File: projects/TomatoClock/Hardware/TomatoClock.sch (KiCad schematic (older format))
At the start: 4 parts, among them U1 ATmega328P-PU, Y1 16MHz

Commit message: TomatoClock: Update hardware schematics
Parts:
- added J1: ICSP, symbol Connector_Generic:Conn_02x03_Odd_Even
- added J2: Screen, Connector_PinHeader_2.00mm:PinHeader_1x04_P2.00mm_Vertical, symbol Connector:Conn_01x04_Male
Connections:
- net +3V3: now also J2.1 (Pin_1)
- net GND: now also J2.2 (Pin_2)
- net SDA: now reaches U1.27 (PC4)
- net SDA: now also J2.3 (Pin_3)
- net SCL: now reaches U1.28 (PC5)
- net SCL: now also J2.4 (Pin_4)
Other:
- note added: "Clock"
- note added: "Peripherals"
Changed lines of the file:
@@
 Wire Notes Line
 	800  750  800  4600
-Wire Notes Line
-	800  4600 4250 4600
-Wire Notes Line
-	4250 4600 4250 750
-Wire Notes Line
-	800  750  4250 750
 Text Notes 3650 4450 0    118  ~ 24
 MCU
+$Comp
+L Connector:Conn_01x04_Male J2
+U 1 1 61928260
+P 5700 1400
+F 0 "J2" H 5672 1374 50  0000 R CNN
+F 1 "Screen" H 5672 1283 50  0000 R CNN
+F 2 "Connector_PinHeader_2.00mm:PinHeader_1x04_P2.00mm_Vertical" H 5700 1400 50  0001 C CNN
+F 3 "~" H 5700 1400 50  0001 C CNN
+	1    5700 1400
+	-1   0    0    -1
+$EndComp
+$Comp
+L power:+3V3 #PWR?
+U 1 1 6192D813
+P 5350 1200
+F 0 "#PWR?" H 5350 1050 50  0001 C CNN
+F 1 "+3V3" H 5365 1373 50  0000 C CNN
+F 2 "" H 5350 1200 50  0001 C CNN
+F 3 "" H 5350 1200 50  0001 C CNN
+	1    5350 1200
+	1    0    0    -1
+$EndComp
+$Comp
+L power:GND #PWR?
+U 1 1 6192DD9D
+P 4900 1500
+F 0 "#PWR?" H 4900 1250 50  0001 C CNN
+F 1 "GND" H 4905 1327 50  0000 C CNN
+F 2 "" H 4900 1500 50  0001 C CNN
+F 3 "" H 4900 1500 50  0001 C CNN
+	1    4900 1500
+	1    0    0    -1
+$EndComp
+Wire Wire Line
+	5350 1200 5350 1300
+Wire Wire Line
+	5350 1300 5500 1300
+Wire Wire Line
+	5500 1400 4900 1400
+Wire Wire Line
+	4900 1400 4900 1500
+Text GLabel 5500 1500 0    39   Input ~ 0
+SDA
+Text GLabel 5500 1600 0    39   Input ~ 0
+SCL
+Wire Notes Line
+	2650 1550 2650 2750
+Wire Notes Line
+	2650 2750 4000 2750
+Wire Notes Line
+	4000 2750 4000 1550
+Wire Notes Line
+	4000 1550 2650 1550
+Text Notes 2700 2700 0    118  ~ 24
+Clock
+Text GLabel 2400 2750 2    39   Input ~ 0
+SDA
+Text GLabel 2400 2850 2    39   Input ~ 0
+SCL
+Wire Notes Line
+	800  4600 4550 4600
+Wire Notes Line
+	4550 750  4550 4600
+Wire Notes Line
+	800  750  4550 750
+$Comp
+L Connector_Generic:Conn_02x03_Odd_Even J1
+U 1 1 6195336E
+P 3650 3800
+F 0 "J1" H 3700 4117 50  0000 C CNN
+F 1 "ICSP" H 3700 4026 50  0000 C CNN
+F 2 "" H 3650 3800 50  0001 C CNN
+F 3 "~" H 3650 3800 50  0001 C CNN
+	1    3650 3800
+	1    0    0    -1
+$EndComp
+Wire Notes Line
+	4650 750  4650 3500
+Wire Notes Line
+	4650 3500 8000 3500
+Wire Notes Line
+	8000 3500 8000 750
+Wire Notes Line
+	8000 750  4650 750
+Text Notes 6900 3400 0    118  ~ 24
+Peripherals
 $EndSCHEMATC

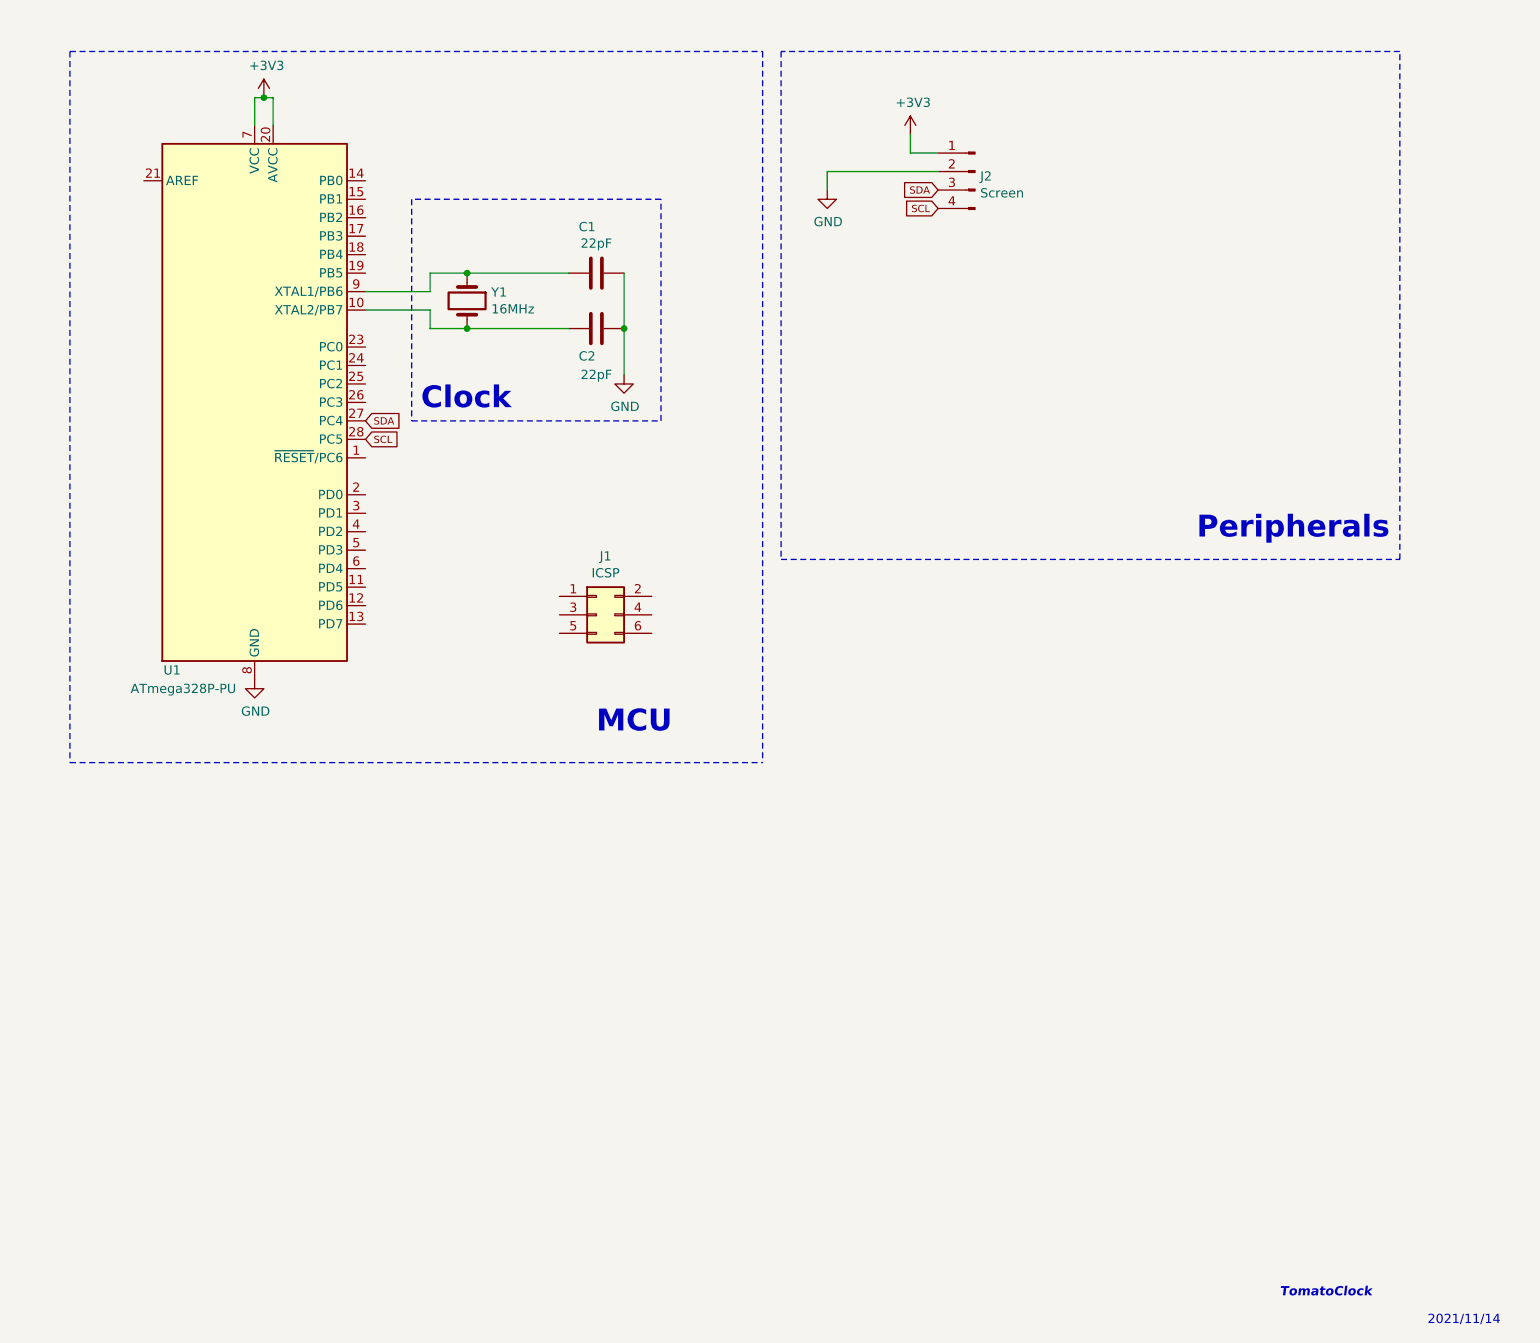
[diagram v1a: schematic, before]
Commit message: TomatoClock: Update hardware
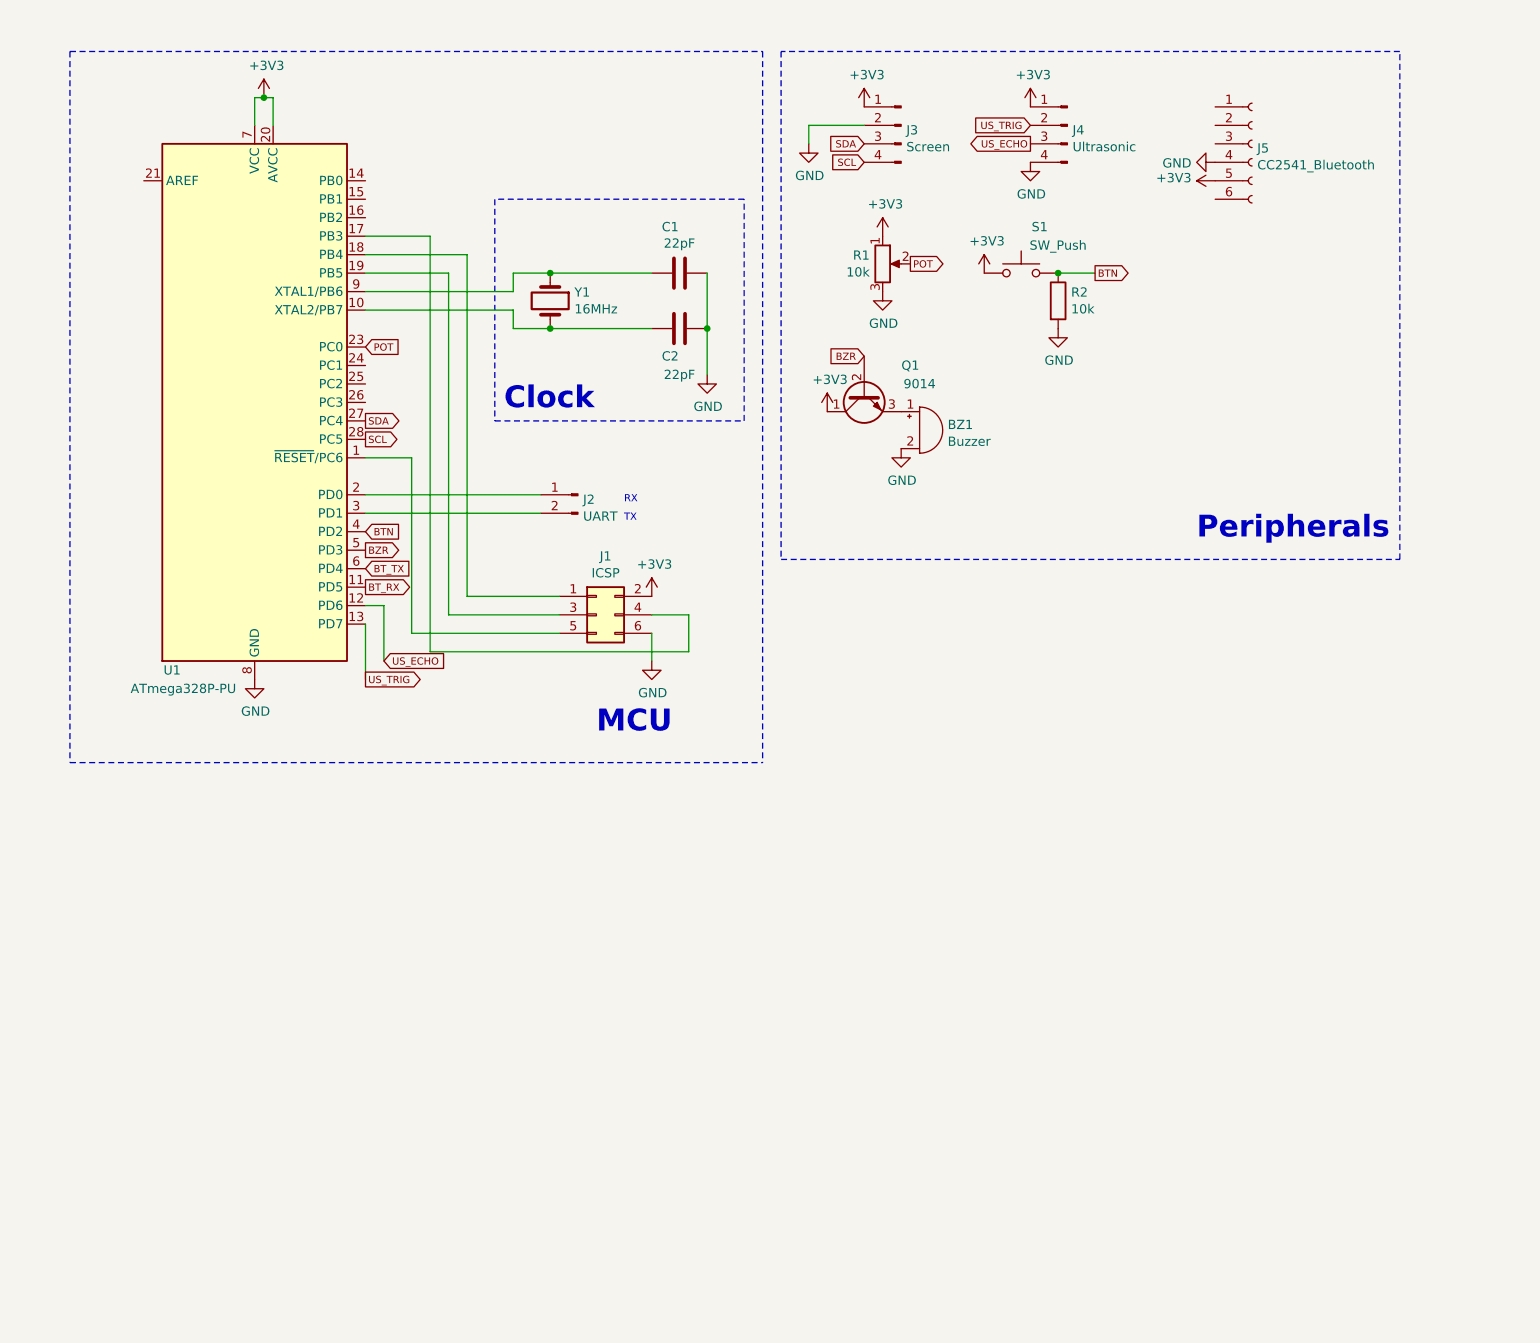
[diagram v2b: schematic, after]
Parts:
- added BZ1: Buzzer, symbol Device:Buzzer
- added J2: UART, symbol Connector:Conn_01x02_Male
- added J4: Ultrasonic, Connector_PinHeader_2.00mm:PinHeader_1x04_P2.00mm_Vertical, symbol Connector:Conn_01x04_Male
- added J5: CC2541_Bluetooth, symbol Connector:Conn_01x06_Female
- added Q1: 9014, Package_TO_SOT_THT:TO-92_HandSolder, symbol Device:Q_NPN_CBE
- added R1: 10k, symbol Device:R_POT
- added R2: 10k, symbol Device:R
- added S1: SW_Push, symbol Switch:SW_Push
- J1: footprint (none) -> Connector_PinHeader_2.00mm:PinHeader_2x03_P2.00mm_Vertical
- renumbered J2 to J3
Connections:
- net +3V3: now also J1.2 (Pin_2), J4.1 (Pin_1), J5.5 (Pin_5), Q1.1 (C), R1.1, S1.1
- net GND: now also J1.6 (Pin_6), BZ1.2 (+), J4.4 (Pin_4), J5.4 (Pin_4), R1.3, R2.2
- net at U1.1 (~RESET~/PC6): now also J1.5 (Pin_5)
- net BT_RX: now reaches U1.11 (PD5)
- net US_ECHO: now reaches U1.12 (PD6)
- net US_ECHO: now also J4.3 (Pin_3)
- net US_TRIG: now reaches U1.13 (PD7)
- net US_TRIG: now also J4.2 (Pin_2)
- net at U1.17 (PB3): now also J1.4 (Pin_4)
- net at U1.18 (PB4): now also J1.1 (Pin_1)
- net at U1.19 (PB5): now also J1.3 (Pin_3)
- net at U1.2 (PD0): now also J2.1 (Pin_1)
- net POT: now reaches U1.23 (PC0)
- net POT: now also R1.2
- net at U1.3 (PD1): now also J2.2 (Pin_2)
- net BTN: now reaches U1.4 (PD2)
- net BTN: now also R2.1, S1.2
- net BZR: now reaches U1.5 (PD3)
- net BZR: now also Q1.2 (B)
- net BT_TX: now reaches U1.6 (PD4)
- new net: BZ1.1 (-), Q1.3 (E)
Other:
- note added: "RX"
- note added: "TX"
- note removed: "2021/11/14"
- note removed: "TomatoClock"
- moved on the sheet: C1, C2, J3, Y1
